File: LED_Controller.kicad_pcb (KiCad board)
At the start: 2 copper layers, 127 x 101.6 mm, 35 parts, among them CON1 CONNECTOR, CON2 CONNECTOR, CON3 CONNECTOR, CON4 CONNECTOR, CON5 PWR_CON, CON6 AVR-ISP-10, CON7 AVR-ISP-6, IC1 ATMEGA328P-P, Q1 STS8DN3LLH5, Q2 STS8DN3LLH5, Q3 STS8DN3LLH5

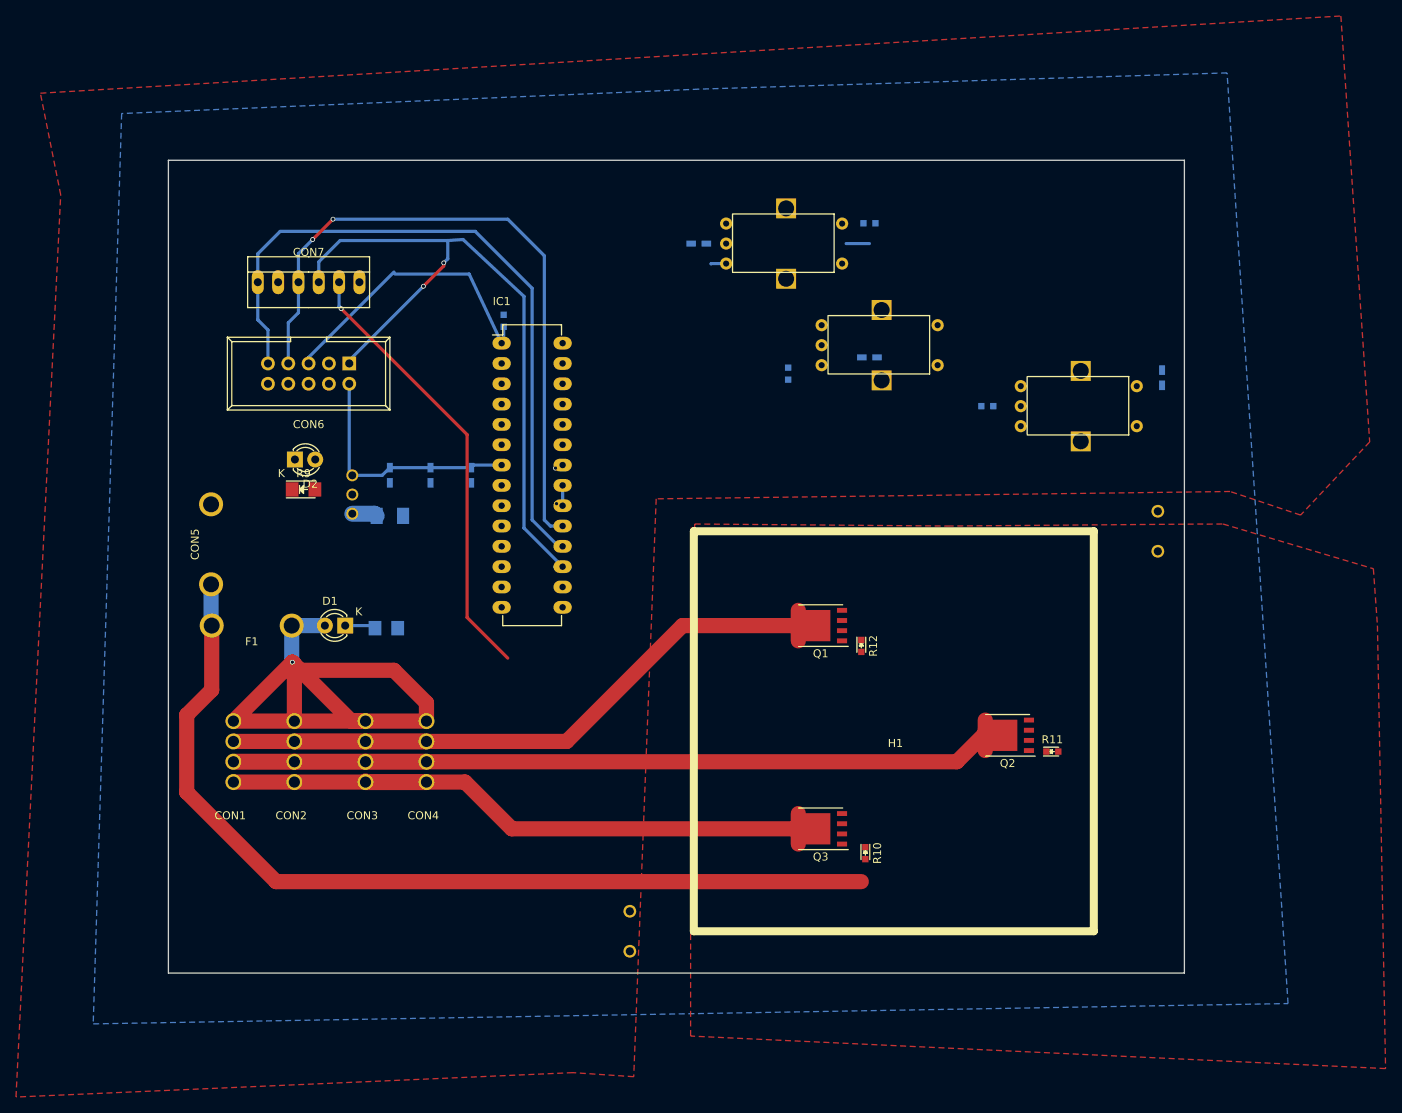
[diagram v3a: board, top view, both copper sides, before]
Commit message: Changed passive sizes, re-routed traces
Changed all passive components to 1206 size (that size is stocked in
the lab, and it should be easier to solder without a scope)

Created a general 1206 footprint for resistors and capacitors

Re-routed traces to MOSFETs and rotary encoders, tried to minimize
number of vias
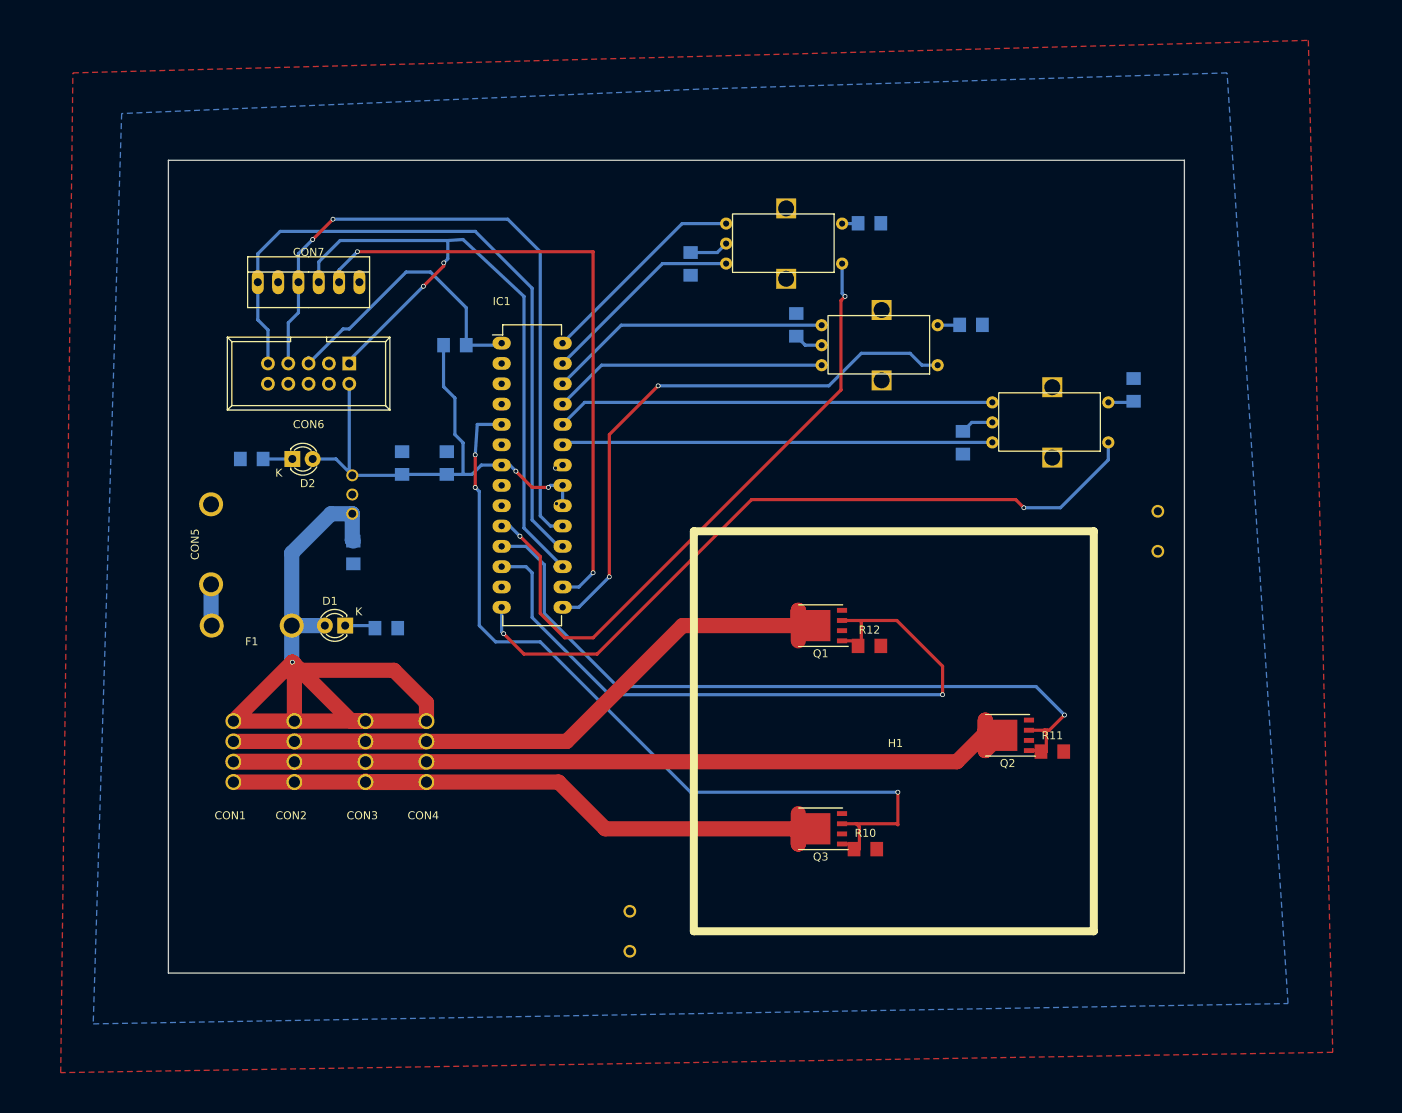
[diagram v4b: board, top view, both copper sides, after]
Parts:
- removed C4: 10uF, Capacitors_SMD:C_0603_HandSoldering
- C1, C2, R3, R4, R5: footprint Capacitors_SMD:C_0603_HandSoldering -> LED_controller_footprints:SMD_1206
- C3: footprint SMD_Packages:SMD-1206_Pol -> LED_controller_footprints:SMD_1206
- R1, R10, R11, R12, R2, R6, R7: footprint LEDs:LED_0603 -> LED_controller_footprints:SMD_1206
- R8: footprint LEDs:LED_1206 -> LED_controller_footprints:SMD_1206
- R9: footprint LEDs:LED_1206 -> LED_controller_footprints:SMD_1206; moved to B.Cu
- moved R5 13.3 mm to (177.8, 72.6)
- moved R9 7.51 mm to (87.9, 89.4), turned to 180 degrees
- moved C2 7.27 mm to (112.3, 89.9), turned to 90 degrees
- moved R7 6.82 mm to (113.3, 75.2), turned to 0 degrees
- moved C3 6.47 mm to (100.6, 101.1), turned to 90 degrees
- moved R2 6.18 mm to (156.0, 72.6), turned to 90 degrees
- moved R1 5.49 mm to (176.8, 87.4), turned to 270 degrees
- moved E1 4.10 mm to (188.0, 84.8)
- moved C1 3.87 mm to (106.7, 89.9), turned to 90 degrees
- moved R4 3.87 mm to (198.1, 80.8)
- moved R3 2.74 mm to (142.7, 65.0), turned to 270 degrees
- moved R12 1.02 mm to (165.1, 112.8), turned to 0 degrees
- moved R10 0.51 mm to (164.6, 138.2), turned to 0 degrees
- moved D2 0.32 mm to (93.0, 89.4)
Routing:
- net Net-(CON5-Pad1): track 116.4 -> 5.31 mm
- net /RED_5V: track 0.00 -> 106.2 mm, vias 0 -> 3
- net /GREEN_5V: track 0.64 -> 94.0 mm, vias 0 -> 1
- net Net-(E1-Pad1): track 0.00 -> 93.1 mm, vias 0 -> 2
- net /BLUE_5V: track 0.25 -> 89.3 mm, vias 0 -> 1
- net Net-(E3-Pad1): track 0.00 -> 81.4 mm, vias 0 -> 2
- net Net-(E2-Pad1): track 0.00 -> 71.1 mm, vias 0 -> 2
- net Net-(E1-Pad5): track 0.00 -> 54.9 mm
- net Net-(E1-Pad4): track 0.00 -> 53.8 mm
- net Net-(E2-Pad5): track 0.00 -> 35.4 mm
- net Net-(E2-Pad4): track 0.00 -> 34.4 mm
- net +5V: track 33.3 -> 65.2 mm, vias 1 -> 3
- net Net-(E3-Pad5): track 0.00 -> 26.6 mm
- net Net-(E3-Pad4): track 2.41 -> 25.6 mm
- net /SS: track 55.7 -> 78.9 mm, vias 1 -> 2
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- removed copper zone on F.Cu, net +12V
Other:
- net class Default: via_dia 0.6 -> 0.8; via_drill 0.4 -> 0.645
- net class HIGH_CURRENT: via_dia 0.6 -> 2.1; via_drill 0.4 -> 1.8
- net class HIGH_CURRENT_NARROW: via_dia 0.6 -> 1.7; via_drill 0.4 -> 1.4

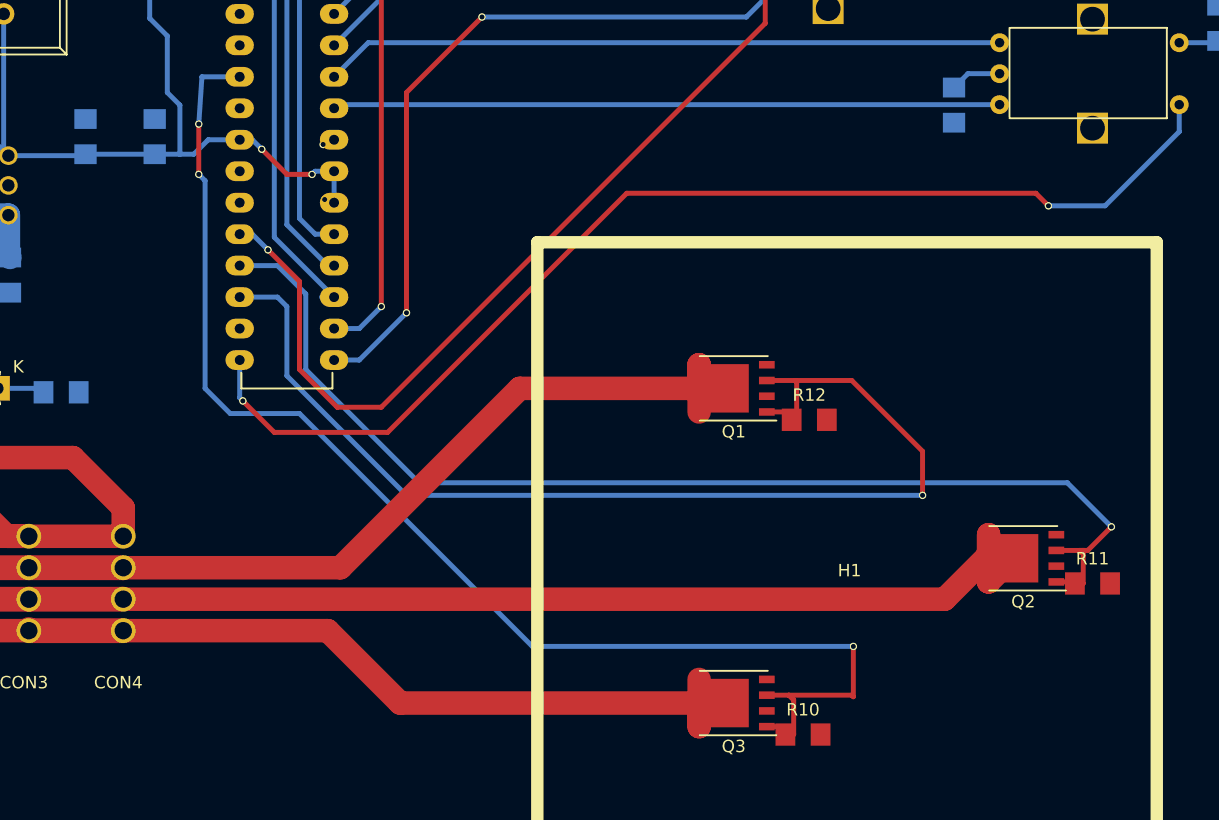
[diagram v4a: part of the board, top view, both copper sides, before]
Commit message: Rewired FETs
corrected incorrectly wired MOSFETs in schematic, updated traces
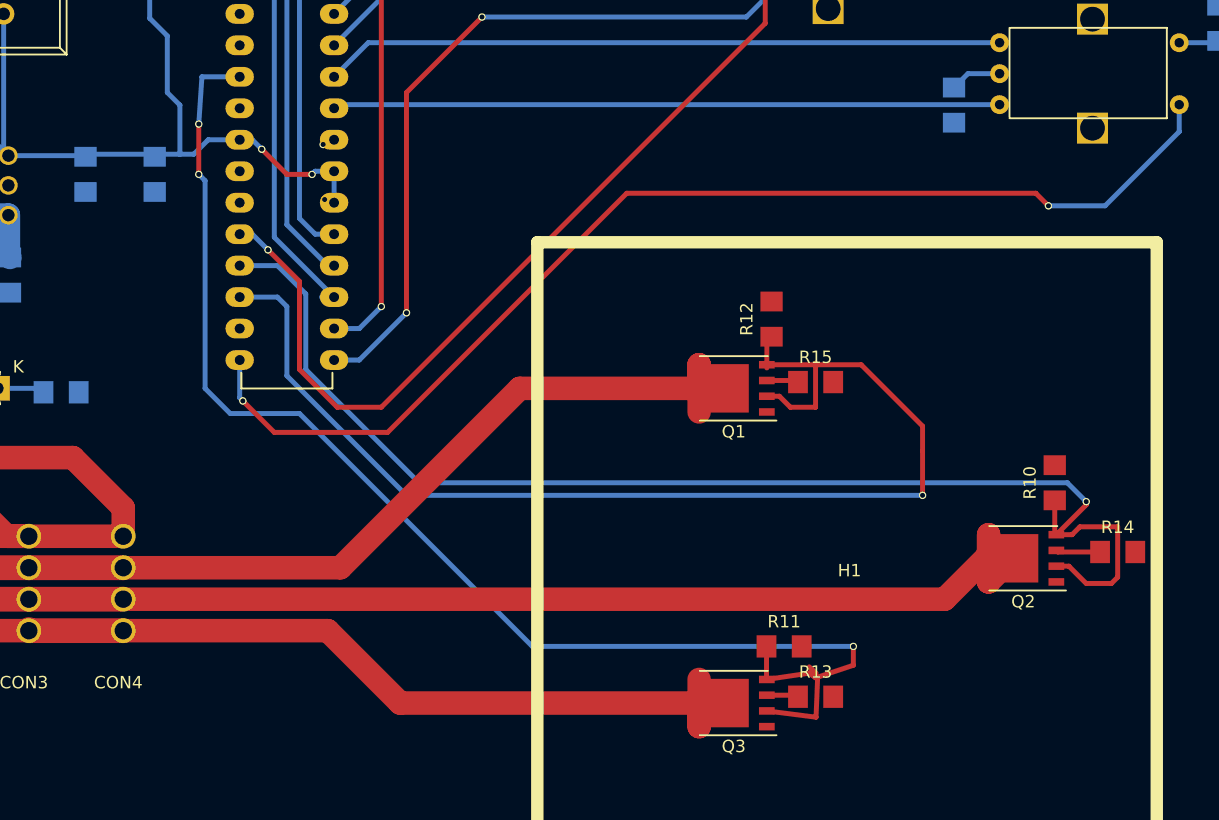
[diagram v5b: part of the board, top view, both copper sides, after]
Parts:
- added R13: 0, LED_controller_footprints:SMD_1206, F.Cu at (165.6, 135.1)
- added R14: 0, LED_controller_footprints:SMD_1206, F.Cu at (190.0, 123.4)
- added R15: 0, LED_controller_footprints:SMD_1206, F.Cu at (165.6, 109.7)
- moved R10 28.7 mm to (184.9, 117.9), turned to 90 degrees
- moved R11 25.4 mm to (163.1, 131.1)
- moved R12 8.68 mm to (162.1, 104.6), turned to 90 degrees
- moved C1 3.05 mm to (106.7, 93.0), turned to 270 degrees
- moved C2 3.05 mm to (112.3, 93.0), turned to 270 degrees
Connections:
- Q1 pad 1: /BLUE_5V -> GND
- Q1 pad 2: GND -> /BLUE_5V
- Q1 pad 3: /BLUE_5V -> GND
- Q1 pad 4: GND -> /BLUE_5V
- Q2 pad 1: /GREEN_5V -> GND
- Q2 pad 2: GND -> /GREEN_5V
- Q2 pad 3: /GREEN_5V -> GND
- Q2 pad 4: GND -> /GREEN_5V
- Q3 pad 1: /RED_5V -> GND
- Q3 pad 2: GND -> /RED_5V
- Q3 pad 3: /RED_5V -> GND
- Q3 pad 4: GND -> /RED_5V
- R10 pad 1: /RED_5V -> /GREEN_5V
- R11 pad 1: /GREEN_5V -> /RED_5V
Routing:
- net GND: track 0.00 -> 8.72 mm
- net /GREEN_5V: track 94.0 -> 101.9 mm
- net /BLUE_5V: track 89.3 -> 95.4 mm
- net /RED_5V: track 106.2 -> 108.1 mm
- net (no net): track 0.00 -> 0.75 mm
